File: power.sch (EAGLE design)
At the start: 7 parts

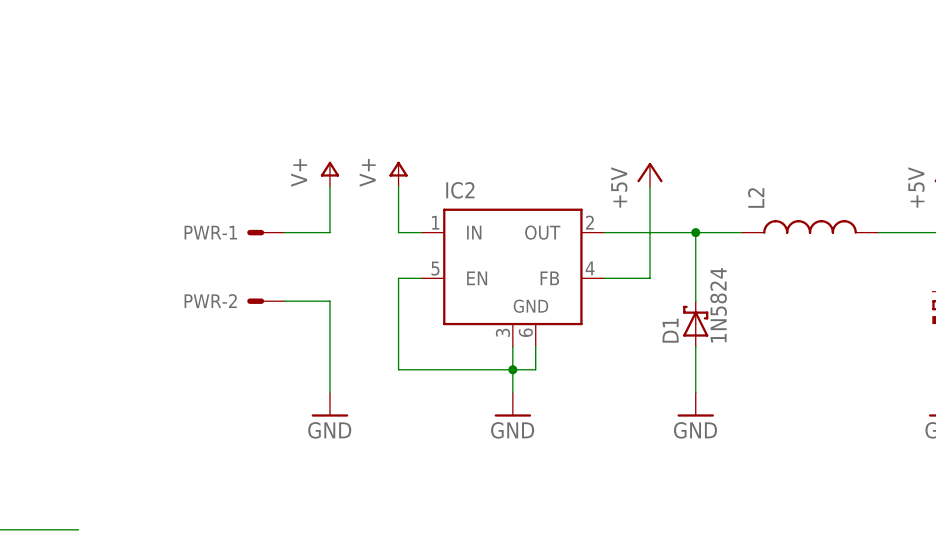
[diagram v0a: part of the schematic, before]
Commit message: Tidy up schematic and part numbers
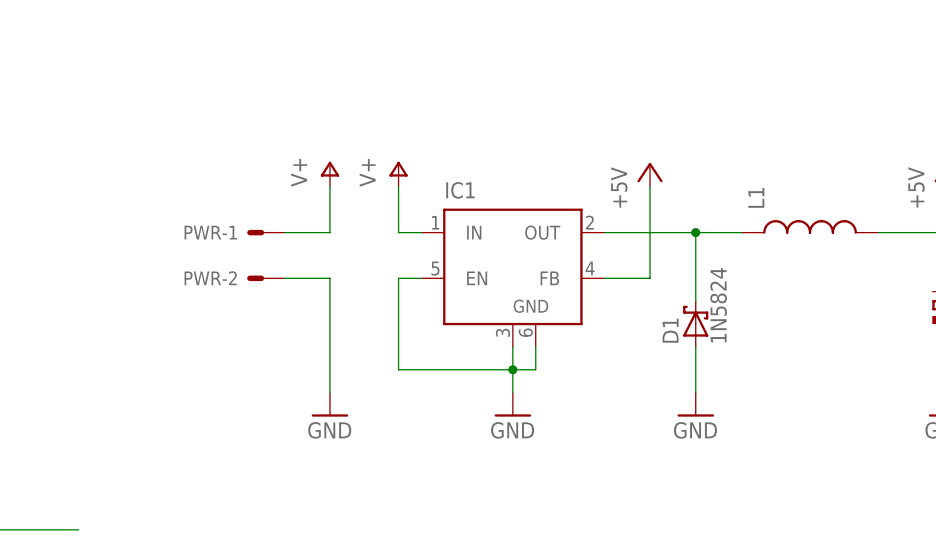
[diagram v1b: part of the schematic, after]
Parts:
- renumbered IC2 to IC1, L2 to L1
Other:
- moved on the sheet: PWR-2
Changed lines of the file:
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@@
 <part name="GND6" library="supply1" deviceset="GND" device=""/>
 <part name="GND8" library="supply1" deviceset="GND" device=""/>
-<part name="IC2" library="linear" deviceset="LM2596S" device=""/>
+<part name="IC1" library="linear" deviceset="LM2596S" device=""/>
 <part name="D1" library="diode" deviceset="1N581*" device="" technology="7-B" value="1N5824"/>
 <part name="P+5" library="supply1" deviceset="+5V" device=""/>
@@
 <part name="C1" library="rcl" deviceset="CPOL-EU" device="E2.5-6" value="680uf"/>
 <part name="PWR" library="con-molex" deviceset="22-?-02" device="05-7028"/>
-<part name="L2" library="SparkFun-Passives" deviceset="INDUCTOR" device="SRU1038"/>
+<part name="L1" library="SparkFun-Passives" deviceset="INDUCTOR" device="SRU1038"/>
 </parts>
 <sheets>
@@
 <instance part="GND6" gate="1" x="86.36" y="15.24"/>
 <instance part="GND8" gate="1" x="114.3" y="15.24"/>
-<instance part="IC2" gate="G$1" x="66.04" y="33.02"/>
+<instance part="IC1" gate="G$1" x="66.04" y="33.02"/>
 <instance part="D1" gate="G$1" x="86.36" y="25.4" rot="R90"/>
 <instance part="P+5" gate="1" x="81.28" y="43.18"/>
@@
 <attribute name="NAME" x="35.56" y="36.322" size="1.524" layer="95" rot="R180"/>
 </instance>
-<instance part="PWR" gate="-2" x="38.1" y="27.94" rot="R180"/>
-<instance part="L2" gate="G$1" x="99.06" y="35.56" rot="R90"/>
+<instance part="PWR" gate="-2" x="38.1" y="30.48" rot="R180"/>
+<instance part="L1" gate="G$1" x="99.06" y="35.56" rot="R90"/>
 </instances>
 <busses>
@@
 </segment>
 <segment>
-<wire x1="40.64" y1="27.94" x2="45.72" y2="27.94" width="0.1524" layer="91"/>
+<wire x1="40.64" y1="30.48" x2="45.72" y2="30.48" width="0.1524" layer="91"/>
 <pinref part="GND11" gate="1" pin="GND"/>
 <pinref part="PWR" gate="-2" pin="S"/>
-<wire x1="45.72" y1="27.94" x2="45.72" y2="17.78" width="0.1524" layer="91"/>
-</segment>
-<segment>
-<pinref part="IC2" gate="G$1" pin="EN"/>
+<wire x1="45.72" y1="30.48" x2="45.72" y2="17.78" width="0.1524" layer="91"/>
+</segment>
+<segment>
+<pinref part="IC1" gate="G$1" pin="EN"/>
 <wire x1="55.88" y1="30.48" x2="53.34" y2="30.48" width="0.1524" layer="91"/>
 <wire x1="53.34" y1="30.48" x2="53.34" y2="20.32" width="0.1524" layer="91"/>
 <wire x1="53.34" y1="20.32" x2="66.04" y2="20.32" width="0.1524" layer="91"/>
-<pinref part="IC2" gate="G$1" pin="GND@1"/>
+<pinref part="IC1" gate="G$1" pin="GND@1"/>
 <wire x1="66.04" y1="20.32" x2="68.58" y2="20.32" width="0.1524" layer="91"/>
 <wire x1="68.58" y1="20.32" x2="68.58" y2="22.86" width="0.1524" layer="91"/>
 <pinref part="GND1" gate="1" pin="GND"/>
 <wire x1="66.04" y1="17.78" x2="66.04" y2="20.32" width="0.1524" layer="91"/>
-<pinref part="IC2" gate="G$1" pin="GND"/>
+<pinref part="IC1" gate="G$1" pin="GND"/>
 <wire x1="66.04" y1="20.32" x2="66.04" y2="22.86" width="0.1524" layer="91"/>
 <junction x="66.04" y="20.32"/>
@@
 <junction x="114.3" y="35.56"/>
 <pinref part="C1" gate="G$1" pin="+"/>
-<pinref part="L2" gate="G$1" pin="2"/>
-</segment>
-<segment>
-<pinref part="IC2" gate="G$1" pin="FB"/>
+<pinref part="L1" gate="G$1" pin="2"/>
+</segment>
+<segment>
+<pinref part="IC1" gate="G$1" pin="FB"/>
 <pinref part="P+5" gate="1" pin="+5V"/>
 <wire x1="76.2" y1="30.48" x2="81.28" y2="30.48" width="0.1524" layer="91"/>
@@
 <pinref part="P+4" gate="1" pin="V+"/>
 <wire x1="53.34" y1="40.64" x2="53.34" y2="35.56" width="0.1524" layer="91"/>
-<pinref part="IC2" gate="G$1" pin="IN"/>
+<pinref part="IC1" gate="G$1" pin="IN"/>
 <wire x1="53.34" y1="35.56" x2="55.88" y2="35.56" width="0.1524" layer="91"/>
 </segment>
@@
 <net name="VOUT" class="0">
 <segment>
-<pinref part="IC2" gate="G$1" pin="OUT"/>
+<pinref part="IC1" gate="G$1" pin="OUT"/>
 <wire x1="76.2" y1="35.56" x2="86.36" y2="35.56" width="0.1524" layer="91"/>
 <wire x1="91.44" y1="35.56" x2="86.36" y2="35.56" width="0.1524" layer="91"/>
@@
 <pinref part="D1" gate="G$1" pin="C"/>
 <junction x="86.36" y="35.56"/>
-<pinref part="L2" gate="G$1" pin="1"/>
-</segment>
-</net>
+<pinref part="L1" gate="G$1" pin="1"/>
+</segment>
+</net>

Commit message: Bits on power
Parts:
- C1: value 680uf -> 220uf
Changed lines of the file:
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@@
 <part name="P+7" library="supply1" deviceset="V+" device=""/>
 <part name="GND11" library="supply1" deviceset="GND" device=""/>
-<part name="C1" library="rcl" deviceset="CPOL-EU" device="E2.5-6" value="680uf"/>
+<part name="C1" library="rcl" deviceset="CPOL-EU" device="E2.5-6" value="220uf"/>
 <part name="PWR" library="con-molex" deviceset="22-?-02" device="05-7028"/>
 <part name="L1" library="SparkFun-Passives" deviceset="INDUCTOR" device="SRU1038"/>
